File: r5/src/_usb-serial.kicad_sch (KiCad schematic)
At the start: 13 parts, among them T41 , U12 CP2102N-Axx-xQFN24

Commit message: Updates to +/-15V supply. Additional output capacitance. Change to smaller inductor packages. Add 0R links to permit isolation of output. Mods to compensation network. Set feedback resistors to datasheet values.
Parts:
- renumbered C39 to C84, C40 to C85, C33 to C86, C132 to C87, C32 to C88, C31 to C89, R25 to R57, R26 to R58, R27 to R59, R28 to R60, U12 to U19

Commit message: Fix broken component annotation by importing back from PCB and fixing duplicates.
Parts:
- renumbered C87 to C132, C89 to C31, C88 to C32, C86 to C33, C84 to C39, C85 to C40, R57 to R25, R58 to R26, R59 to R27, R60 to R28, U19 to U12
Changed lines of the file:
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@@
   (symbol (lib_id "Device:R_Small") (at 127 74.93 0) (unit 1)
     (in_bom yes) (on_board yes) (dnp no)
-    (property "Reference" "R60" (at 128.905 74.295 0)
+    (property "Reference" "R28" (at 128.905 74.295 0)
       (effects (font (size 1.27 1.27)) (justify left))
     )
@@
       (project "bugg-main-r5"
         (path "/e3eb514f-6ce4-4abe-ba20-f82f0015628f/26331aa8-35b7-4c22-8a42-89230ada1085"
-          (reference "R60") (unit 1)
+          (reference "R28") (unit 1)
         )
       )
@@
   (symbol (lib_id "Device:C") (at 154.94 62.23 0) (unit 1)
     (in_bom yes) (on_board yes) (dnp no)
-    (property "Reference" "C86" (at 157.861 61.0616 0)
+    (property "Reference" "C33" (at 157.861 61.0616 0)
       (effects (font (size 1.27 1.27)) (justify left))
     )
@@
       (project "bugg-main-r5"
         (path "/e3eb514f-6ce4-4abe-ba20-f82f0015628f/26331aa8-35b7-4c22-8a42-89230ada1085"
-          (reference "C86") (unit 1)
+          (reference "C33") (unit 1)
         )
       )
@@
   (symbol (lib_id "Device:C") (at 168.91 62.23 0) (unit 1)
     (in_bom yes) (on_board yes) (dnp no)
-    (property "Reference" "C87" (at 171.831 61.0616 0)
+    (property "Reference" "C132" (at 171.831 61.0616 0)
       (effects (font (size 1.27 1.27)) (justify left))
     )
@@
       (project "bugg-main-r5"
         (path "/e3eb514f-6ce4-4abe-ba20-f82f0015628f/26331aa8-35b7-4c22-8a42-89230ada1085"
-          (reference "C87") (unit 1)
+          (reference "C132") (unit 1)
         )
       )
@@
   (symbol (lib_id "Device:C") (at 101.6 86.36 0) (mirror y) (unit 1)
     (in_bom yes) (on_board yes) (dnp no)
-    (property "Reference" "C84" (at 98.679 85.1916 0)
+    (property "Reference" "C39" (at 98.679 85.1916 0)
       (effects (font (size 1.27 1.27)) (justify left))
     )
@@
       (project "bugg-main-r5"
         (path "/e3eb514f-6ce4-4abe-ba20-f82f0015628f/26331aa8-35b7-4c22-8a42-89230ada1085"
-          (reference "C84") (unit 1)
+          (reference "C39") (unit 1)
         )
       )
@@
   (symbol (lib_id "Device:C") (at 176.53 80.01 0) (mirror y) (unit 1)
     (in_bom yes) (on_board yes) (dnp no)
-    (property "Reference" "C88" (at 173.609 78.8416 0)
+    (property "Reference" "C32" (at 173.609 78.8416 0)
       (effects (font (size 1.27 1.27)) (justify left))
     )
@@
       (project "bugg-main-r5"
         (path "/e3eb514f-6ce4-4abe-ba20-f82f0015628f/26331aa8-35b7-4c22-8a42-89230ada1085"
-          (reference "C88") (unit 1)
+          (reference "C32") (unit 1)
         )
       )
@@
   (symbol (lib_id "Device:R_Small") (at 120.65 110.49 0) (unit 1)
     (in_bom yes) (on_board yes) (dnp no)
-    (property "Reference" "R58" (at 122.555 109.855 0)
+    (property "Reference" "R26" (at 122.555 109.855 0)
       (effects (font (size 1.27 1.27)) (justify left))
     )
@@
       (project "bugg-main-r5"
         (path "/e3eb514f-6ce4-4abe-ba20-f82f0015628f/26331aa8-35b7-4c22-8a42-89230ada1085"
-          (reference "R58") (unit 1)
+          (reference "R26") (unit 1)
         )
       )
@@
   (symbol (lib_id "Device:R_Small") (at 120.65 93.98 0) (unit 1)
     (in_bom yes) (on_board yes) (dnp no)
-    (property "Reference" "R57" (at 122.555 93.345 0)
+    (property "Reference" "R25" (at 122.555 93.345 0)
       (effects (font (size 1.27 1.27)) (justify left))
     )
@@
       (project "bugg-main-r5"
         (path "/e3eb514f-6ce4-4abe-ba20-f82f0015628f/26331aa8-35b7-4c22-8a42-89230ada1085"
-          (reference "R57") (unit 1)
+          (reference "R25") (unit 1)
         )
       )
@@
   (symbol (lib_id "Device:C") (at 110.49 86.36 0) (unit 1)
     (in_bom yes) (on_board yes) (dnp no)
-    (property "Reference" "C85" (at 113.411 85.1916 0)
+    (property "Reference" "C40" (at 113.411 85.1916 0)
       (effects (font (size 1.27 1.27)) (justify left))
     )
@@
       (project "bugg-main-r5"
         (path "/e3eb514f-6ce4-4abe-ba20-f82f0015628f/26331aa8-35b7-4c22-8a42-89230ada1085"
-          (reference "C85") (unit 1)
+          (reference "C40") (unit 1)
         )
       )
@@
         )
         (path "/e3eb514f-6ce4-4abe-ba20-f82f0015628f/26331aa8-35b7-4c22-8a42-89230ada1085"
-          (reference "T24") (unit 1)
+          (reference "T53") (unit 1)
         )
       )
@@
   (symbol (lib_id "Device:R_Small") (at 120.65 116.84 0) (unit 1)
     (in_bom yes) (on_board yes) (dnp no)
-    (property "Reference" "R59" (at 122.555 116.205 0)
+    (property "Reference" "R27" (at 122.555 116.205 0)
       (effects (font (size 1.27 1.27)) (justify left))
     )
@@
       (project "bugg-main-r5"
         (path "/e3eb514f-6ce4-4abe-ba20-f82f0015628f/26331aa8-35b7-4c22-8a42-89230ada1085"
-          (reference "R59") (unit 1)
+          (reference "R27") (unit 1)
         )
       )
@@
   (symbol (lib_id "Interface_USB:CP2102N-Axx-xQFN24") (at 143.51 110.49 0) (unit 1)
     (in_bom yes) (on_board yes) (dnp no)
-    (property "Reference" "U19" (at 148.59 140.97 0)
+    (property "Reference" "U12" (at 148.59 140.97 0)
       (effects (font (size 1.27 1.27)))
     )
@@
       (project "bugg-main-r5"
         (path "/e3eb514f-6ce4-4abe-ba20-f82f0015628f/26331aa8-35b7-4c22-8a42-89230ada1085"
-          (reference "U19") (unit 1)
+          (reference "U12") (unit 1)
         )
       )
@@
   (symbol (lib_id "Device:C") (at 185.42 80.01 0) (unit 1)
     (in_bom yes) (on_board yes) (dnp no)
-    (property "Reference" "C89" (at 188.341 78.8416 0)
+    (property "Reference" "C31" (at 188.341 78.8416 0)
       (effects (font (size 1.27 1.27)) (justify left))
     )
@@
       (project "bugg-main-r5"
         (path "/e3eb514f-6ce4-4abe-ba20-f82f0015628f/26331aa8-35b7-4c22-8a42-89230ada1085"
-          (reference "C89") (unit 1)
+          (reference "C31") (unit 1)
         )
       )
@@
         )
         (path "/e3eb514f-6ce4-4abe-ba20-f82f0015628f/26331aa8-35b7-4c22-8a42-89230ada1085"
-          (reference "T25") (unit 1)
-        )
-      )
+          (reference "T54") (unit 1)
+        )
+      )

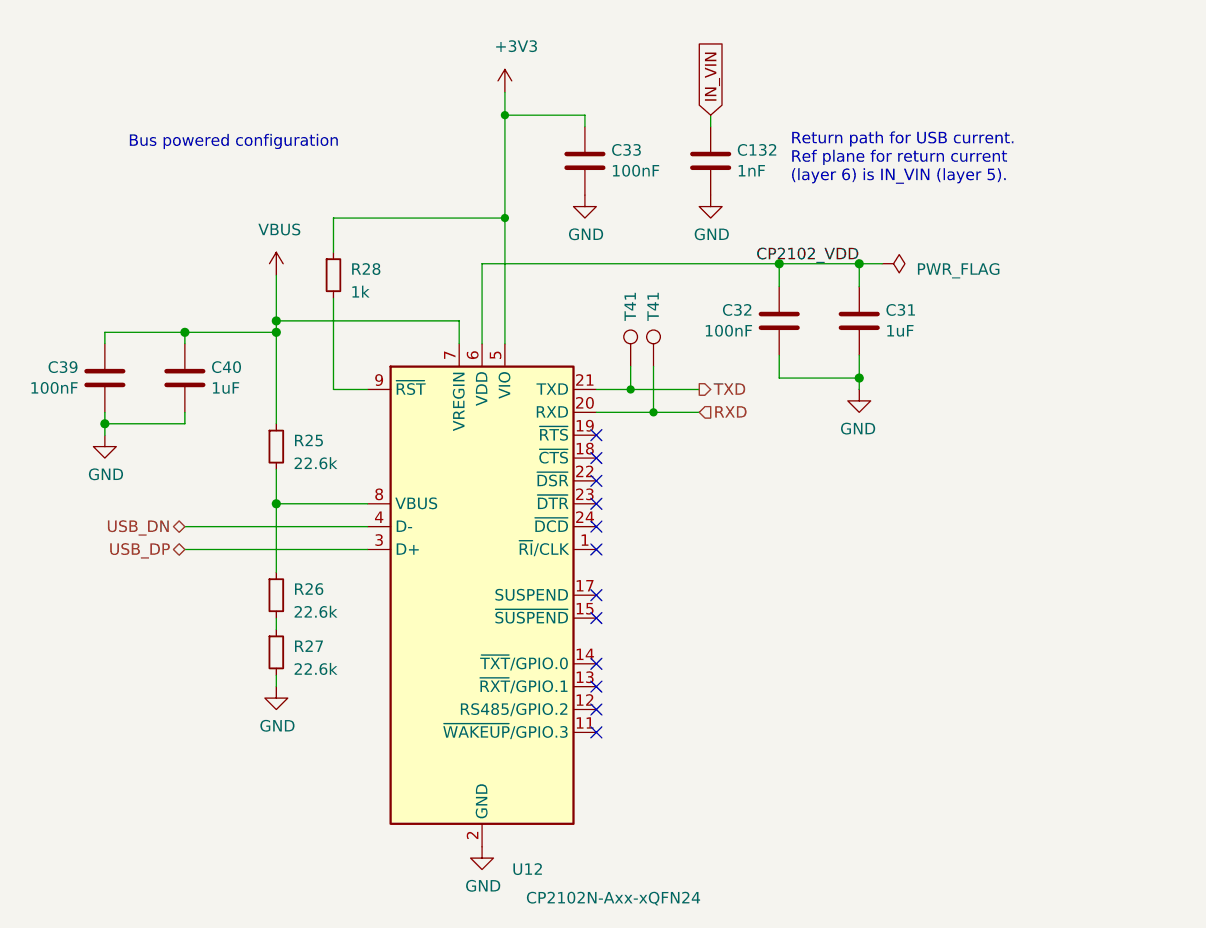
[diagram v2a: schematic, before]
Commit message: Change CP2102 power connections to prevent latch-up when P3.3V phantom is enabled and USB is disconnected
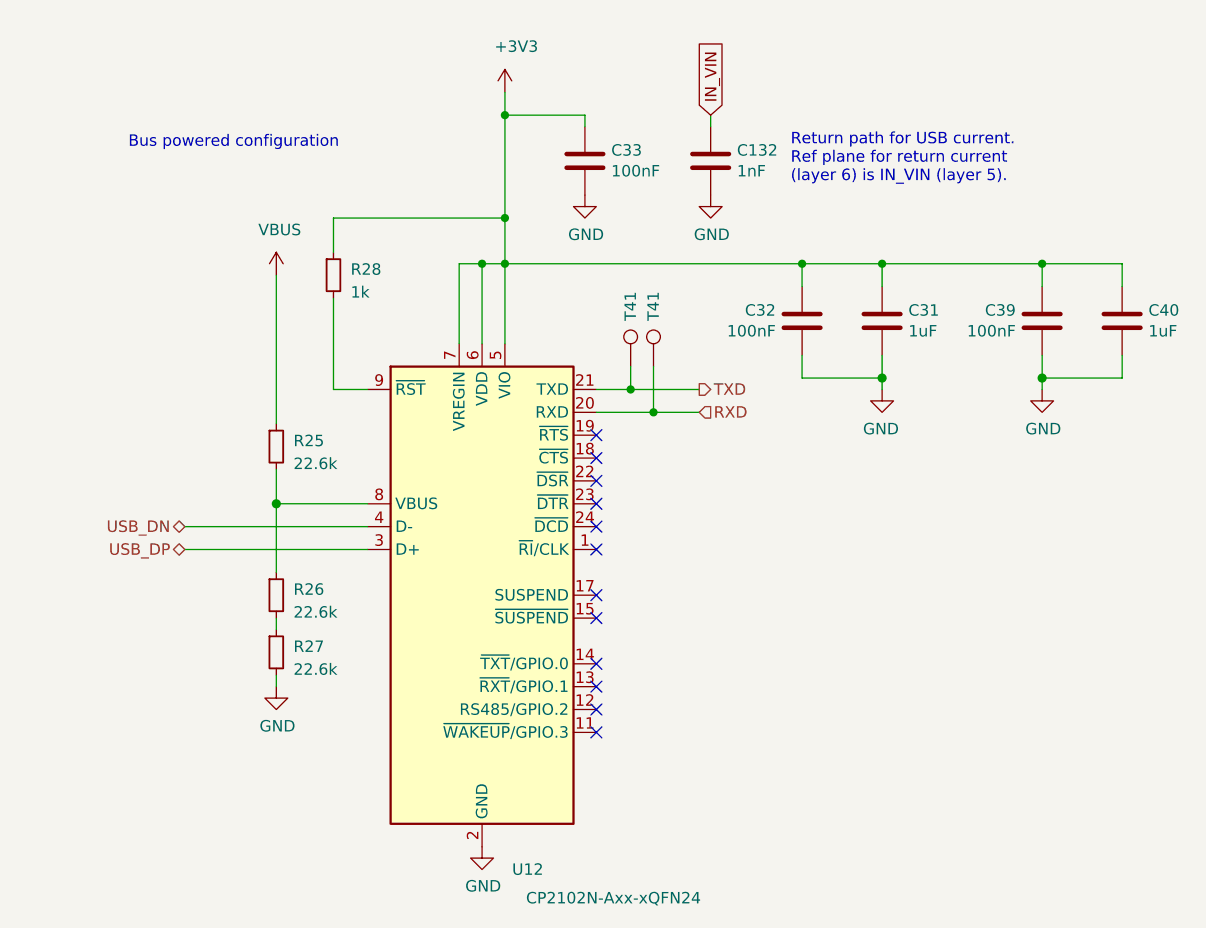
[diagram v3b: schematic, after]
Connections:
- net CP2102_VDD is gone; now on net +3V3: C31.1, C32.1, U12.6 (VDD)
- net +3V3: now also C39.1, C40.1, U12.7 (VREGIN)
- net VBUS: no longer C39.1, C40.1, U12.7 (VREGIN)
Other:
- moved on the sheet: C31, C32, C39, C40

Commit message: Change 0805 47uF to 1206 to save a BOM line. Update layout, DRC pass.
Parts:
- C31, C40: MPN (none) -> GRM155C81C105KE15D; Manufacturer (none) -> Murata; Mouser (none) -> 81-GRM155C81C105KE5D
- C32, C33, C39: MPN (none) -> GRM155R71H104KE14D; Manufacturer (none) -> Murata; Mouser (none) -> 81-GRM155R71H104KE4D; Voltage (none) -> 50V
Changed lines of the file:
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@@
+      (effects (font (size 1.27 1.27)) hide)
+    )
+    (property "Digikey" "" (at 127 74.93 0)
+      (effects (font (size 1.27 1.27)) hide)
+    )
+    (property "MPN" "" (at 127 74.93 0)
+      (effects (font (size 1.27 1.27)) hide)
+    )
+    (property "Mouser" "" (at 127 74.93 0)
+      (effects (font (size 1.27 1.27)) hide)
+    )
+    (property "Field-1" "" (at 127 74.93 0)
       (effects (font (size 1.27 1.27)) hide)
     )
@@
       (effects (font (size 1.27 1.27)) hide)
     )
+    (property "Digikey" "" (at 154.94 62.23 0)
+      (effects (font (size 1.27 1.27)) hide)
+    )
+    (property "MPN" "GRM155R71H104KE14D " (at 154.94 62.23 0)
+      (effects (font (size 1.27 1.27)) hide)
+    )
+    (property "Mouser" "81-GRM155R71H104KE4D " (at 154.94 62.23 0)
+      (effects (font (size 1.27 1.27)) hide)
+    )
+    (property "Field-1" "" (at 154.94 62.23 0)
+      (effects (font (size 1.27 1.27)) hide)
+    )
+    (property "Manufacturer" "Murata" (at 154.94 62.23 0)
+      (effects (font (size 1.27 1.27)) hide)
+    )
+    (property "Voltage" "50V" (at 154.94 62.23 0)
+      (effects (font (size 1.27 1.27)) hide)
+    )
     (pin "1")
     (pin "2")
@@
       (effects (font (size 1.27 1.27)) hide)
     )
+    (property "Digikey" "" (at 168.91 62.23 0)
+      (effects (font (size 1.27 1.27)) hide)
+    )
+    (property "MPN" "" (at 168.91 62.23 0)
+      (effects (font (size 1.27 1.27)) hide)
+    )
+    (property "Mouser" "" (at 168.91 62.23 0)
+      (effects (font (size 1.27 1.27)) hide)
+    )
+    (property "Field-1" "" (at 168.91 62.23 0)
+      (effects (font (size 1.27 1.27)) hide)
+    )
     (pin "1")
     (pin "2")
@@
       (effects (font (size 1.27 1.27)) hide)
     )
+    (property "Digikey" "" (at 205.74 80.01 0)
+      (effects (font (size 1.27 1.27)) hide)
+    )
+    (property "MPN" "GRM155R71H104KE14D " (at 205.74 80.01 0)
+      (effects (font (size 1.27 1.27)) hide)
+    )
+    (property "Mouser" "81-GRM155R71H104KE4D " (at 205.74 80.01 0)
+      (effects (font (size 1.27 1.27)) hide)
+    )
+    (property "Field-1" "" (at 205.74 80.01 0)
+      (effects (font (size 1.27 1.27)) hide)
+    )
+    (property "Manufacturer" "Murata" (at 205.74 80.01 0)
+      (effects (font (size 1.27 1.27)) hide)
+    )
+    (property "Voltage" "50V" (at 205.74 80.01 0)
+      (effects (font (size 1.27 1.27)) hide)
+    )
     (pin "1")
     (pin "2")
@@
       (effects (font (size 1.27 1.27)) hide)
     )
+    (property "Digikey" "" (at 179.07 80.01 0)
+      (effects (font (size 1.27 1.27)) hide)
+    )
+    (property "MPN" "GRM155R71H104KE14D " (at 179.07 80.01 0)
+      (effects (font (size 1.27 1.27)) hide)
+    )
+    (property "Mouser" "81-GRM155R71H104KE4D " (at 179.07 80.01 0)
+      (effects (font (size 1.27 1.27)) hide)
+    )
+    (property "Field-1" "" (at 179.07 80.01 0)
+      (effects (font (size 1.27 1.27)) hide)
+    )
+    (property "Manufacturer" "Murata" (at 179.07 80.01 0)
+      (effects (font (size 1.27 1.27)) hide)
+    )
+    (property "Voltage" "50V" (at 179.07 80.01 0)
+      (effects (font (size 1.27 1.27)) hide)
+    )
     (pin "1")
     (pin "2")
@@
       (effects (font (size 1.27 1.27)) hide)
     )
+    (property "Digikey" "" (at 120.65 110.49 0)
+      (effects (font (size 1.27 1.27)) hide)
+    )
+    (property "MPN" "" (at 120.65 110.49 0)
+      (effects (font (size 1.27 1.27)) hide)
+    )
+    (property "Mouser" "" (at 120.65 110.49 0)
+      (effects (font (size 1.27 1.27)) hide)
+    )
+    (property "Field-1" "" (at 120.65 110.49 0)
+      (effects (font (size 1.27 1.27)) hide)
+    )
     (pin "1")
     (pin "2")
@@
       (effects (font (size 1.27 1.27)) hide)
     )
+    (property "Digikey" "" (at 120.65 93.98 0)
+      (effects (font (size 1.27 1.27)) hide)
+    )
+    (property "MPN" "" (at 120.65 93.98 0)
+      (effects (font (size 1.27 1.27)) hide)
+    )
+    (property "Mouser" "" (at 120.65 93.98 0)
+      (effects (font (size 1.27 1.27)) hide)
+    )
+    (property "Field-1" "" (at 120.65 93.98 0)
+      (effects (font (size 1.27 1.27)) hide)
+    )
     (pin "1")
     (pin "2")
@@
       (effects (font (size 1.27 1.27)) hide)
     )
+    (property "Digikey" "" (at 214.63 80.01 0)
+      (effects (font (size 1.27 1.27)) hide)
+    )
+    (property "MPN" "GRM155C81C105KE15D" (at 214.63 80.01 0)
+      (effects (font (size 1.27 1.27)) hide)
+    )
+    (property "Mouser" "81-GRM155C81C105KE5D " (at 214.63 80.01 0)
+      (effects (font (size 1.27 1.27)) hide)
+    )
+    (property "Field-1" "" (at 214.63 80.01 0)
+      (effects (font (size 1.27 1.27)) hide)
+    )
+    (property "Manufacturer" "Murata" (at 214.63 80.01 0)
+      (effects (font (size 1.27 1.27)) hide)
+    )
     (pin "1")
     (pin "2")
@@
     )
     (property "Quantity" "" (at 160.02 85.09 0)
+      (effects (font (size 1.27 1.27)) hide)
+    )
+    (property "Digikey" "" (at 160.02 85.09 0)
+      (effects (font (size 1.27 1.27)) hide)
+    )
+    (property "MPN" "" (at 160.02 85.09 0)
+      (effects (font (size 1.27 1.27)) hide)
+    )
+    (property "Mouser" "" (at 160.02 85.09 0)
+      (effects (font (size 1.27 1.27)) hide)
+    )
+    (property "Field-1" "" (at 160.02 85.09 0)
       (effects (font (size 1.27 1.27)) hide)
     )
@@
       (effects (font (size 1.27 1.27)) hide)
     )
+    (property "Digikey" "" (at 120.65 116.84 0)
+      (effects (font (size 1.27 1.27)) hide)
+    )
+    (property "MPN" "" (at 120.65 116.84 0)
+      (effects (font (size 1.27 1.27)) hide)
+    )
+    (property "Mouser" "" (at 120.65 116.84 0)
+      (effects (font (size 1.27 1.27)) hide)
+    )
+    (property "Field-1" "" (at 120.65 116.84 0)
+      (effects (font (size 1.27 1.27)) hide)
+    )
     (pin "1")
     (pin "2")
@@
     )
     (property "Quantity" "" (at 143.51 110.49 0)
+      (effects (font (size 1.27 1.27)) hide)
+    )
+    (property "Digikey" "" (at 143.51 110.49 0)
+      (effects (font (size 1.27 1.27)) hide)
+    )
+    (property "MPN" "" (at 143.51 110.49 0)
+      (effects (font (size 1.27 1.27)) hide)
+    )
+    (property "Mouser" "" (at 143.51 110.49 0)
+      (effects (font (size 1.27 1.27)) hide)
+    )
+    (property "Field-1" "" (at 143.51 110.49 0)
       (effects (font (size 1.27 1.27)) hide)
     )
@@
       (effects (font (size 1.27 1.27)) hide)
     )
+    (property "Digikey" "" (at 187.96 80.01 0)
+      (effects (font (size 1.27 1.27)) hide)
+    )
+    (property "MPN" "GRM155C81C105KE15D" (at 187.96 80.01 0)
+      (effects (font (size 1.27 1.27)) hide)
+    )
+    (property "Mouser" "81-GRM155C81C105KE5D " (at 187.96 80.01 0)
+      (effects (font (size 1.27 1.27)) hide)
+    )
+    (property "Field-1" "" (at 187.96 80.01 0)
+      (effects (font (size 1.27 1.27)) hide)
+    )
+    (property "Manufacturer" "Murata" (at 187.96 80.01 0)
+      (effects (font (size 1.27 1.27)) hide)
+    )
     (pin "1")
     (pin "2")
@@
       (effects (font (size 1.27 1.27)) hide)
     )
+    (property "Digikey" "" (at 162.56 85.09 0)
+      (effects (font (size 1.27 1.27)) hide)
+    )
+    (property "MPN" "" (at 162.56 85.09 0)
+      (effects (font (size 1.27 1.27)) hide)
+    )
+    (property "Mouser" "" (at 162.56 85.09 0)
+      (effects (font (size 1.27 1.27)) hide)
+    )
+    (property "Field-1" "" (at 162.56 85.09 0)
+      (effects (font (size 1.27 1.27)) hide)
+    )
